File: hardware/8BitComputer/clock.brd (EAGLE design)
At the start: 127 x 50.5 mm, 11 parts, among them IC1 LM555CN, J1 Power

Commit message: just need to route
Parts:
- added C4, C5, C6: 0.1 uF, passives:C0805
- added J2: Clock Output, connector:1X06
- added LED2: Green, leds:LED3MM-NS
- added LED3: White, leds:LED3MM-NS
- added Q1, Q2: P2N2222AZL1G, transitors:2N6027
- added R5: 4.7 K, passives:0805
- added R6, R7: 100 R, passives:0805
- added R8, R9: 1 K, passives:0805
- added S1: 555 or Manual, switches:SWITCH-SPDT_KIT
- added S2: Halt, switches:SWITCH-SPDT_KIT
- added U$2: SWITCH_TACTILETACTILE_PIN, switches:TACTILE-PTH
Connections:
- new net CLOCK_OUT: C6.2, J2.1, J2.2, J2.3, J2.4, J2.5, J2.6, Q2.3, R7.2
- new net MANUAL_TIMER: C4.1, LED2.A, S1.1, U$2.1, U$2.2
- new net N$10: Q1.3, Q2.1
- new net N$11: R8.2, S2.2
- new net N$12: Q1.2, R9.2
- new net N$5: LED2.K, R6.1
- new net N$6: R5.1, U$2.3, U$2.4
- new net N$7: LED3.K, R7.1
- new net N$8: Q2.2, S2.1
- new net SWITCHED_CLOCK_OUT: C5.2, R9.1, S1.2
- net 555-1-OUT: now also S1.3
- net GND: now also C4.2, C5.1, C6.1, Q1.1, R6.2
- net VCC5V: now also LED3.A, R5.2, R8.1

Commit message: organized board
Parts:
- added J3: (no value), connector:1X08
- added J4, J5: Power, connector:1X02
- J2: value Clock Output -> Power; device connector:1X06 -> connector:1X02
- moved C6 40.7 mm to (74.9, 17.8), turned to 90 degrees
- moved LED3 29.9 mm to (82.5, 11.4), turned to 90 degrees
- moved R9 22.4 mm to (60.1, 23.9), turned to 270 degrees
- moved J1 21.6 mm to (3.81, 1.27), turned to 0 degrees
- moved R7 20.3 mm to (82.5, 17.8), turned to 90 degrees
- moved C5 19.5 mm to (60.8, 27.9), turned to 180 degrees
- moved Q1 18.2 mm to (76.2, 36.8), turned to 270 degrees
- moved S1 16.3 mm to (54.6, 27.9)
- moved U$1 10.9 mm to (16.5, 40.6)
- moved R6 9.92 mm to (44.5, 41.9)
- moved S2 8.98 mm to (96.5, 17.8)
- moved R8 8.89 mm to (102.9, 17.8)
- moved LED2 8.26 mm to (44.8, 34.9), turned to 90 degrees
- moved R2 7.73 mm to (11.4, 35.6)
- moved U$2 6.84 mm to (35.6, 33.0), turned to 180 degrees
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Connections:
- net CLOCK_OUT: now also J3.2, J3.3, J3.4, J3.5, J3.6, J3.7; no longer J2.1, J2.2, J2.3, J2.4, J2.5, J2.6
- net GND: now also J2.2, J3.8, J4.2, J5.2
- net VCC5V: now also J2.1, J3.1, J4.1, J5.1
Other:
- board size 127 x 50.5 mm -> 127 x 50.8 mm

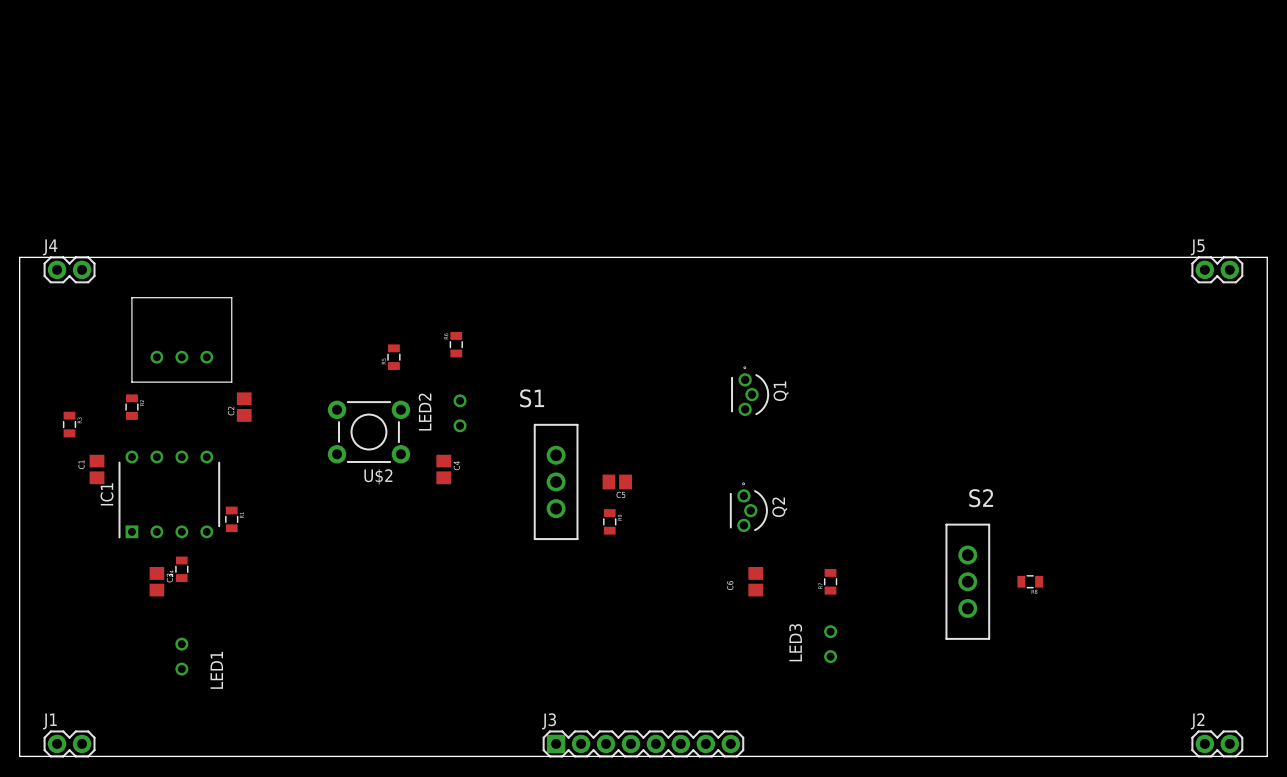
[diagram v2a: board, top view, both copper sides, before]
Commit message: Sons first Routed Board
Using ground plane on 2nd side of board to make layout easier.
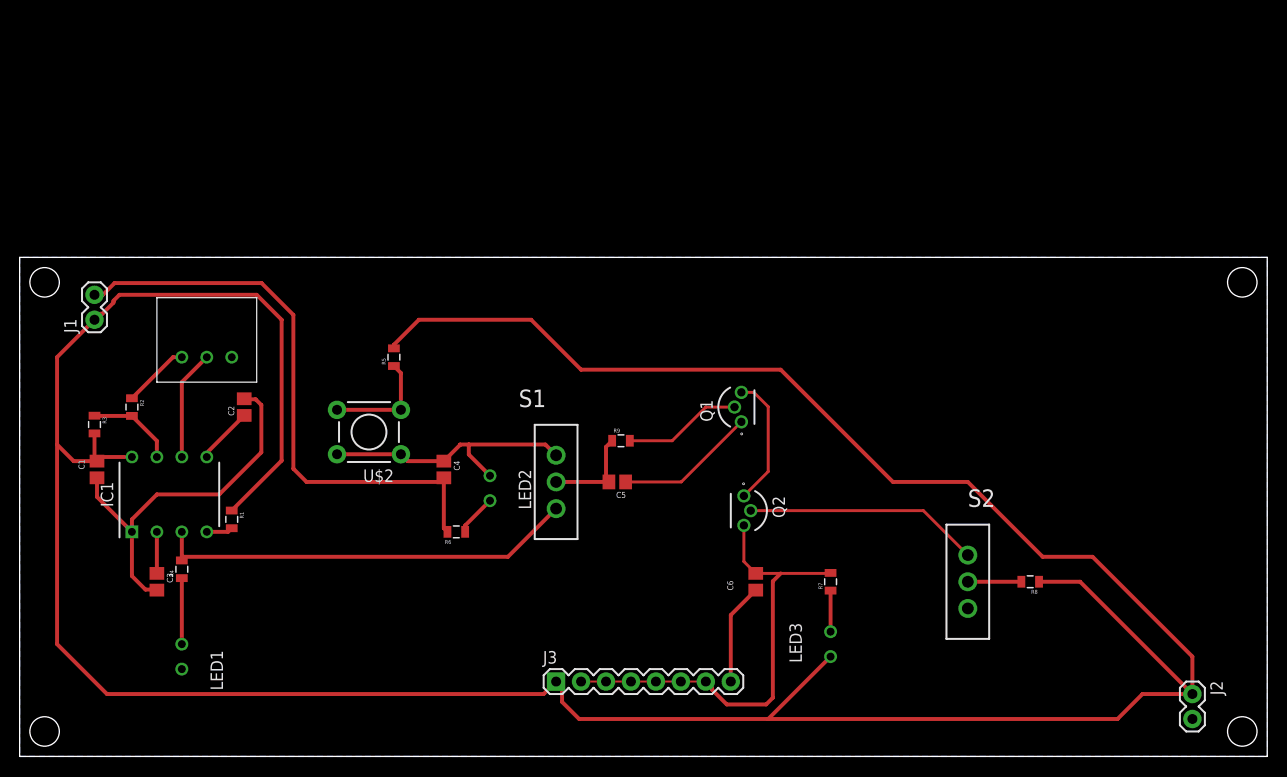
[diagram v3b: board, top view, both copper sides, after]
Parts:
- removed J4, J5: Power, connector:1X02
- moved J1 43.3 mm to (7.62, 44.5), turned to 90 degrees
- moved R6 19.0 mm to (44.5, 22.9), turned to 180 degrees
- moved R9 8.33 mm to (61.2, 32.1), turned to 0 degrees
- moved LED2 8.21 mm to (47.9, 27.3), turned to 270 degrees
- moved J3 6.35 mm to (54.6, 7.62)
- moved J2 5.24 mm to (119.4, 6.35), turned to 270 degrees
- moved Q1 5.24 mm to (71.1, 35.6), turned to 90 degrees
- moved R3 2.54 mm to (7.62, 33.8)
- moved U$1 2.54 mm to (19.1, 40.6)
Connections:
- net GND: no longer J4.2, J5.2
- net VCC5V: no longer J4.1, J5.1
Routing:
- net VCC5V: track 0.00 -> 340.5 mm
- net GND: track 0.00 -> 122.8 mm
- net CLOCK_OUT: track 0.00 -> 46.9 mm
- net 555-1-OUT: track 0.00 -> 43.0 mm
- net MANUAL_TIMER: track 0.00 -> 27.8 mm
- net N$8: track 0.00 -> 24.0 mm
- net N$10: track 0.00 -> 13.4 mm
- net N$12: track 0.00 -> 12.1 mm
- net N$6: track 0.00 -> 11.3 mm
- net THRESHOLD_TRIGGER: track 0.00 -> 11.2 mm
- net SWITCHED_CLOCK_OUT: track 0.00 -> 9.82 mm
- net DISCHARGE: track 0.00 -> 9.05 mm
- net N$3: track 0.00 -> 6.81 mm
- net N$4: track 0.00 -> 6.72 mm
- net N$2: track 0.00 -> 5.81 mm
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- added copper zone on layer 16, net GND

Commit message: thicked traces: moved the resitor on halt switch so it can be pull up or pull down
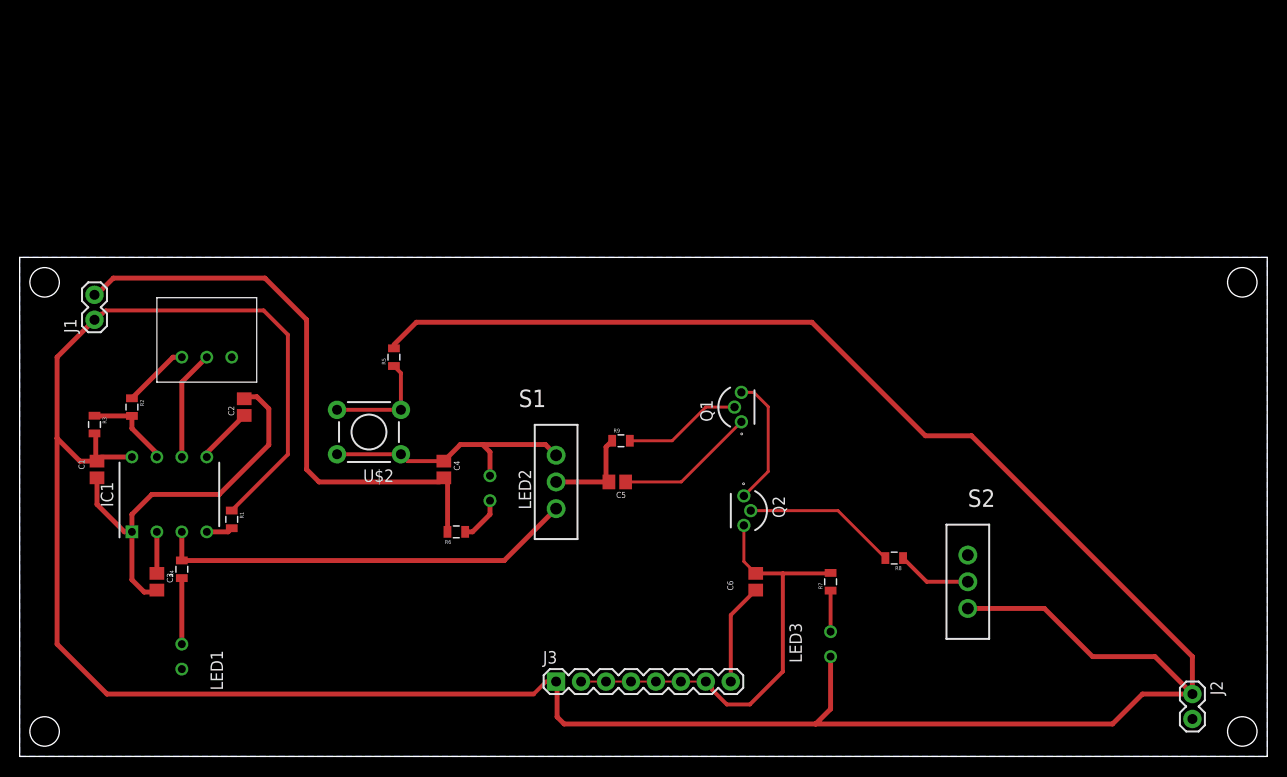
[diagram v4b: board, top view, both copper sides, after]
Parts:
- moved R8 14.1 mm to (89.0, 20.2)
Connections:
- removed net N$11: R8.2, S2.2
- new net N$9: Q2.2, R8.2
- net GND: now also S2.1
- net N$8: now also R8.1, S2.2; no longer Q2.2, S2.1
- net VCC5V: now also S2.3; no longer R8.1
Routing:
- net N$8: track 24.0 -> 7.59 mm
- net N$9: track 0.00 -> 15.7 mm
- net N$11: track 5.45 -> 0.00 mm
- net VCC5V: track 340.5 -> 345.4 mm
- net GND: track 122.8 -> 125.2 mm
- net CLOCK_OUT: track 46.9 -> 46.0 mm
- net MANUAL_TIMER: track 27.8 -> 27.3 mm

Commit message: lay out for size of our FR-4 boards
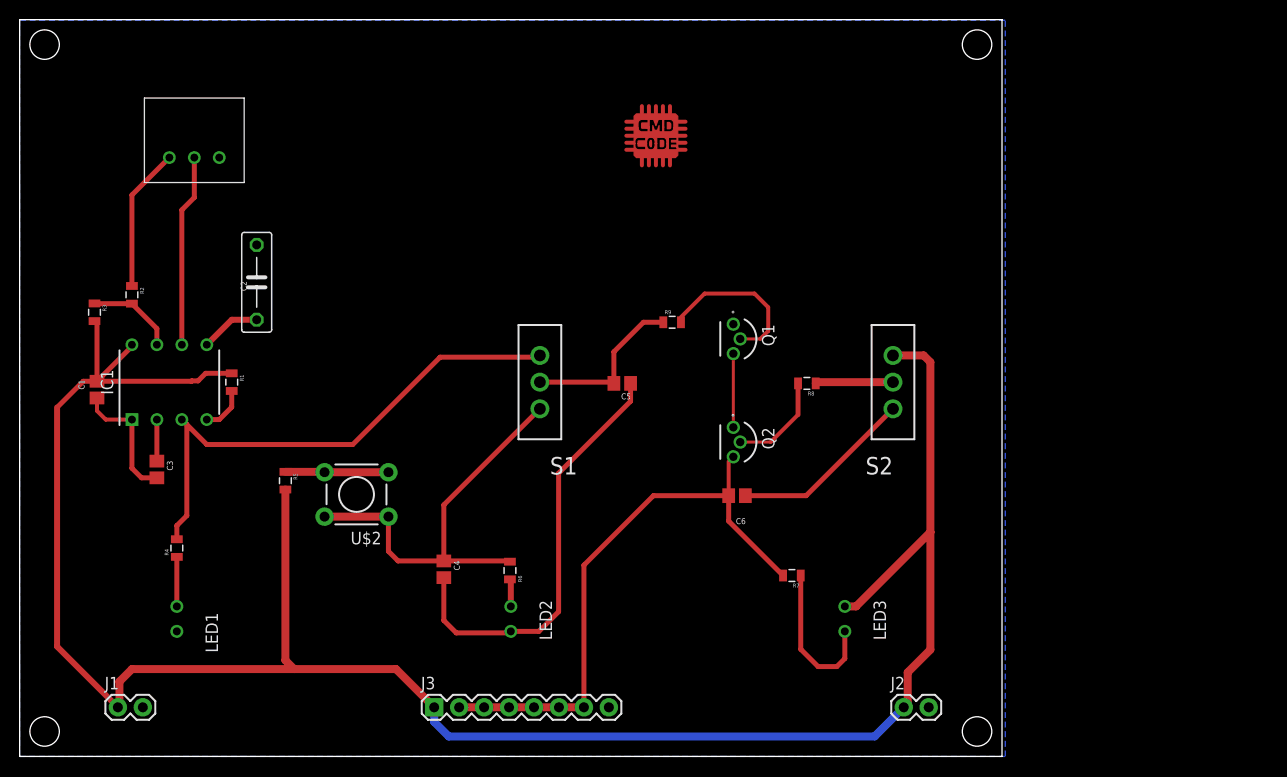
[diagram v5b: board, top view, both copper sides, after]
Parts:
- added U$3: CMD_C0DE_LOGOCMD_CODE_LOGO_TOP_COPPER, logos:CMD_C0DE_LOGO_TOP_COPPER
- C2: device passives:C0805 -> passives:C075-032X103
- moved J1 39.5 mm to (10.0, 5.00), turned to 0 degrees
- moved J2 29.4 mm to (90.0, 5.00), turned to 0 degrees
- moved S2 21.7 mm to (88.9, 38.1), turned to 180 degrees
- moved U$1 20.4 mm to (17.8, 61.0)
- moved R8 19.9 mm to (80.1, 38.0)
- moved R5 16.7 mm to (27.1, 28.1), turned to 270 degrees
- moved R1 14.0 mm to (21.6, 38.1)
- moved LED2 13.5 mm to (50.0, 14.0)
- moved R9 13.1 mm to (66.4, 44.2)
- moved C2 12.8 mm to (24.1, 48.3)
- moved J3 12.7 mm to (42.2, 5.00)
- moved R3 11.4 mm to (7.62, 45.2)
- moved C3 11.4 mm to (14.0, 29.2)
- moved IC1 11.4 mm to (15.2, 38.1)
- moved R2 11.4 mm to (11.4, 47.0)
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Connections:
- net GND: now also LED2.K; no longer R6.2
- net MANUAL_TIMER: now also R6.1; no longer LED2.A
- net N$5: now also LED2.A, R6.2; no longer LED2.K, R6.1
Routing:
- net VCC5V: track 345.4 -> 222.6 mm
- net GND: track 125.2 -> 75.6 mm
- net MANUAL_TIMER: track 27.3 -> 42.4 mm
- net CLOCK_OUT: track 46.0 -> 59.4 mm
- net N$7: track 4.18 -> 15.8 mm
- net 555-1-OUT: track 43.2 -> 54.1 mm
- net THRESHOLD_TRIGGER: track 11.2 -> 19.6 mm
- net N$3: track 6.81 -> 14.6 mm
- net SWITCHED_CLOCK_OUT: track 9.82 -> 17.1 mm
- net N$10: track 13.4 -> 7.50 mm
- net N$9: track 15.7 -> 10.2 mm
- net N$12: track 12.1 -> 16.6 mm
- net N$1: track 2.69 -> 4.71 mm
- net N$5: track 4.66 -> 2.79 mm
- net N$4: track 6.72 -> 5.04 mm
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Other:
- board size 127 x 50.8 mm -> 100 x 75 mm

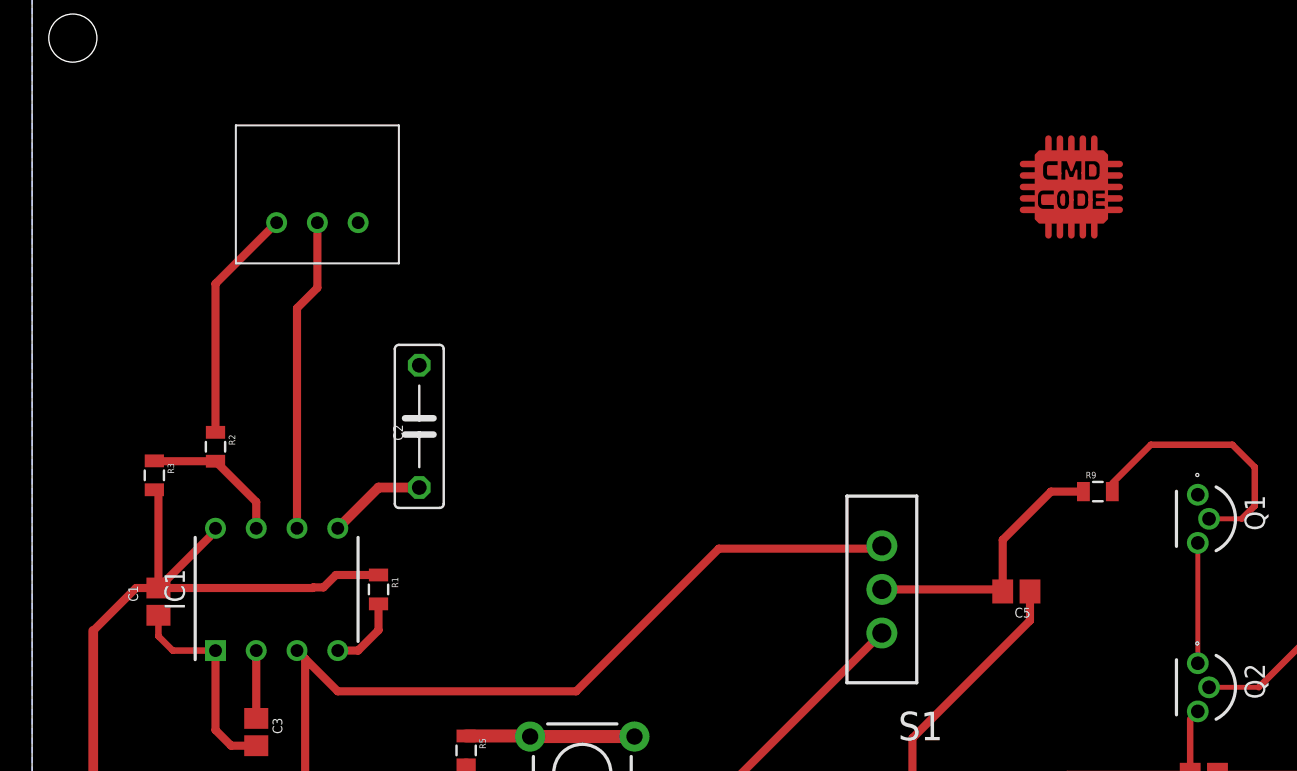
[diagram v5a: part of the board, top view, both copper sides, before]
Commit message: fixed missing trace on 555- miss spelled threshold :(
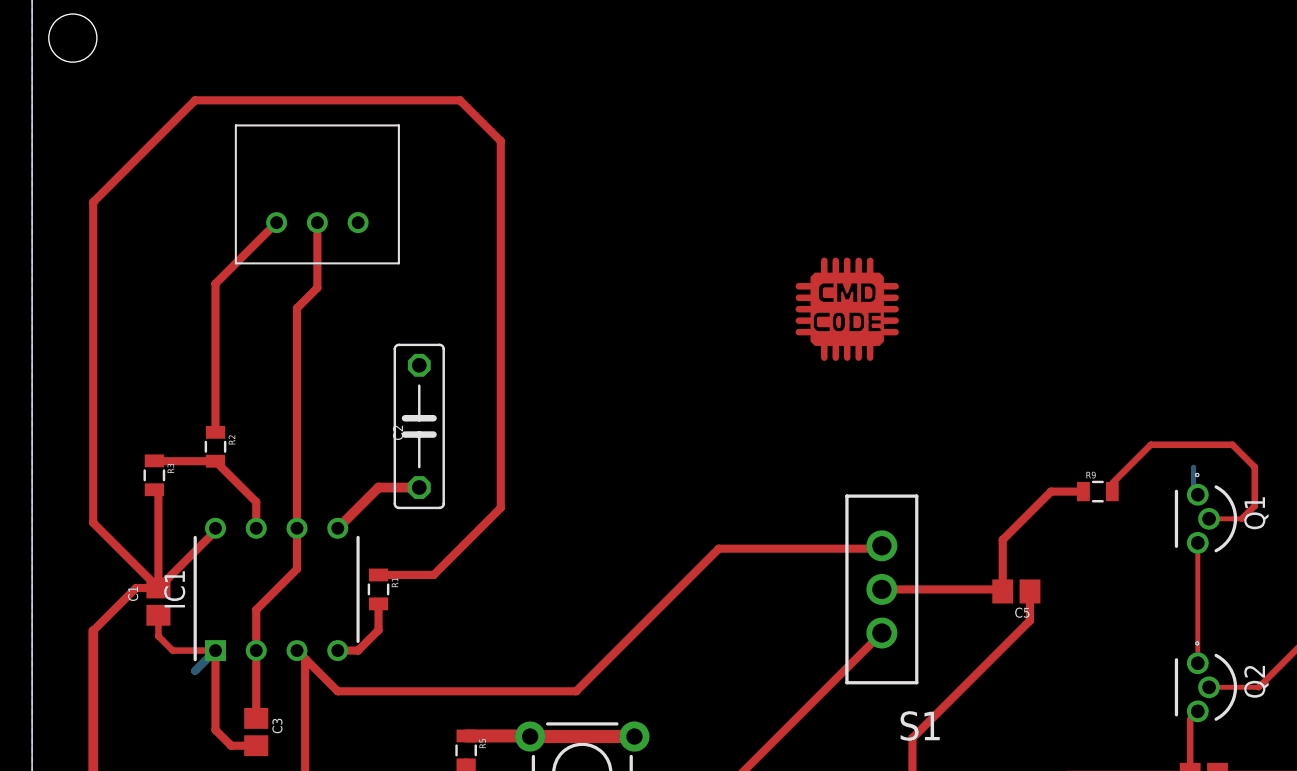
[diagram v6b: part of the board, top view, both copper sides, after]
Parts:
- C3: value 1 uF -> 3.3 uF
- J3: value (none) -> CLK_OUTS
- moved U$3 15.9 mm to (50.8, 55.9)
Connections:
- removed net TRESHOLD_TRIGGER: C3.1, IC1.2
- net THRESHOLD_TRIGGER: now also C3.1, IC1.2
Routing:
- net VCC5V: track 222.6 -> 295.5 mm
- net THRESHOLD_TRIGGER: track 19.6 -> 32.5 mm
- net TRESHOLD_TRIGGER: track 4.23 -> 0.00 mm
- net GND: track 75.6 -> 79.2 mm
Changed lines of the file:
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@@
 <attribute name="VALUE" x="25.908" y="47.117" size="0.6096" layer="27" font="vector" rot="R90"/>
 </element>
-<element name="C3" library="passives" package="C0805" value="1 uF" x="13.97" y="29.21" smashed="yes" rot="R270">
+<element name="C3" library="passives" package="C0805" value="3.3 uF" x="13.97" y="29.21" smashed="yes" rot="R270">
 <attribute name="NAME" x="14.986" y="30.099" size="0.6096" layer="25" font="vector" rot="R270"/>
 <attribute name="VALUE" x="12.192" y="30.353" size="0.6096" layer="27" font="vector" rot="R270"/>
@@
 <attribute name="VALUE" x="74.168" y="28.321" size="0.6096" layer="27" font="vector" rot="R180"/>
 </element>
-<element name="J3" library="connector" package="1X08" value="" x="42.2" y="5" smashed="yes">
+<element name="J3" library="connector" package="1X08" value="CLK_OUTS" x="42.2" y="5" smashed="yes">
 <attribute name="NAME" x="40.8538" y="6.8288" size="1.27" layer="25" ratio="10"/>
 <attribute name="PROD_ID" value="CONN-08438" x="42.2" y="5" size="1.778" layer="27" display="off"/>
@@
 <attribute name="VALUE" x="88.73" y="1.825" size="1.27" layer="27"/>
 </element>
-<element name="U$3" library="logos" package="CMD_C0DE_LOGO_TOP_COPPER" value="CMD_C0DE_LOGOCMD_CODE_LOGO_TOP_COPPER" x="64.77" y="63.5" smashed="yes"/>
+<element name="U$3" library="logos" package="CMD_C0DE_LOGO_TOP_COPPER" value="CMD_C0DE_LOGOCMD_CODE_LOGO_TOP_COPPER" x="50.8" y="55.88" smashed="yes"/>
 </elements>
 <signals>
@@
 <wire x1="17.78" y1="56.896" x2="17.78" y2="60.96" width="0.508" layer="1"/>
 <wire x1="16.51" y1="55.626" x2="17.78" y2="56.896" width="0.508" layer="1"/>
+<contactref element="IC1" pad="2"/>
+<contactref element="C3" pad="1"/>
+<wire x1="13.97" y1="34.29" x2="13.97" y2="30.06" width="0.508" layer="1"/>
+<wire x1="13.97" y1="34.29" x2="13.97" y2="36.83" width="0.508" layer="1"/>
+<wire x1="13.97" y1="36.83" x2="16.51" y2="39.37" width="0.508" layer="1"/>
+<wire x1="16.51" y1="39.37" x2="16.51" y2="41.91" width="0.508" layer="1"/>
 </signal>
 <signal name="VCC5V">
@@
 <wire x1="7.874" y1="38.188" x2="11.43" y2="41.744" width="0.508" layer="1"/>
 <wire x1="11.43" y1="41.744" x2="11.43" y2="41.91" width="0.508" layer="1"/>
-<wire x1="7.874" y1="38.188" x2="17.487" y2="38.188" width="0.508" layer="1"/>
-<wire x1="17.487" y1="38.188" x2="17.526" y2="38.227" width="0.508" layer="1"/>
-<wire x1="17.526" y1="38.227" x2="18.161" y2="38.227" width="0.508" layer="1"/>
-<wire x1="18.934" y1="39" x2="21.59" y2="39" width="0.508" layer="1"/>
-<wire x1="18.161" y1="38.227" x2="18.934" y2="39" width="0.508" layer="1"/>
 <wire x1="88.9" y1="40.8178" x2="92.0242" y2="40.8178" width="0.8128" layer="1"/>
 <wire x1="92.0242" y1="40.8178" x2="92.71" y2="40.132" width="0.8128" layer="1"/>
 <wire x1="92.71" y1="40.132" x2="92.71" y2="22.837" width="0.8128" layer="1"/>
+<wire x1="7.874" y1="38.188" x2="3.81" y2="42.252" width="0.508" layer="1"/>
+<wire x1="3.81" y1="42.252" x2="3.81" y2="62.23" width="0.508" layer="1"/>
+<wire x1="3.81" y1="62.23" x2="10.16" y2="68.58" width="0.508" layer="1"/>
+<wire x1="10.16" y1="68.58" x2="26.67" y2="68.58" width="0.508" layer="1"/>
+<wire x1="26.67" y1="68.58" x2="29.21" y2="66.04" width="0.508" layer="1"/>
+<wire x1="29.21" y1="66.04" x2="29.21" y2="43.18" width="0.508" layer="1"/>
+<wire x1="29.21" y1="43.18" x2="25.03" y2="39" width="0.508" layer="1"/>
+<wire x1="25.03" y1="39" x2="21.59" y2="39" width="0.508" layer="1"/>
 </signal>
 <signal name="GND" airwireshidden="yes">
@@
 <contactref element="J3" pad="8"/>
 <contactref element="J2" pad="2"/>
-<polygon width="0.4" layer="16" isolate="1.27">
+<polygon width="0.4" layer="16" isolate="1.9304">
 <vertex x="0" y="74.93"/>
 <vertex x="0" y="0"/>
@@
 <wire x1="12.407" y1="28.36" x2="11.43" y2="29.337" width="0.508" layer="1"/>
 <wire x1="11.43" y1="29.337" x2="11.43" y2="34.29" width="0.508" layer="1"/>
+<wire x1="11.43" y1="34.29" x2="10.16" y2="33.02" width="0.508" layer="16"/>
+<wire x1="72.65" y1="44" x2="72.39" y2="44.26" width="0.3048" layer="16"/>
+<wire x1="72.39" y1="44.26" x2="72.39" y2="45.72" width="0.3048" layer="16"/>
 </signal>
 <signal name="N$1">
@@
 <wire x1="21.59" y1="44.45" x2="24.13" y2="44.45" width="0.6096" layer="1"/>
 </signal>
-<signal name="TRESHOLD_TRIGGER">
-<contactref element="IC1" pad="2"/>
-<contactref element="C3" pad="1"/>
-<wire x1="13.97" y1="34.29" x2="13.97" y2="30.06" width="0.508" layer="1"/>
-</signal>
 <signal name="555-1-OUT">
